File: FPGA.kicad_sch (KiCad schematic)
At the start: 8 parts, among them U3 XC7A100T-FTG256

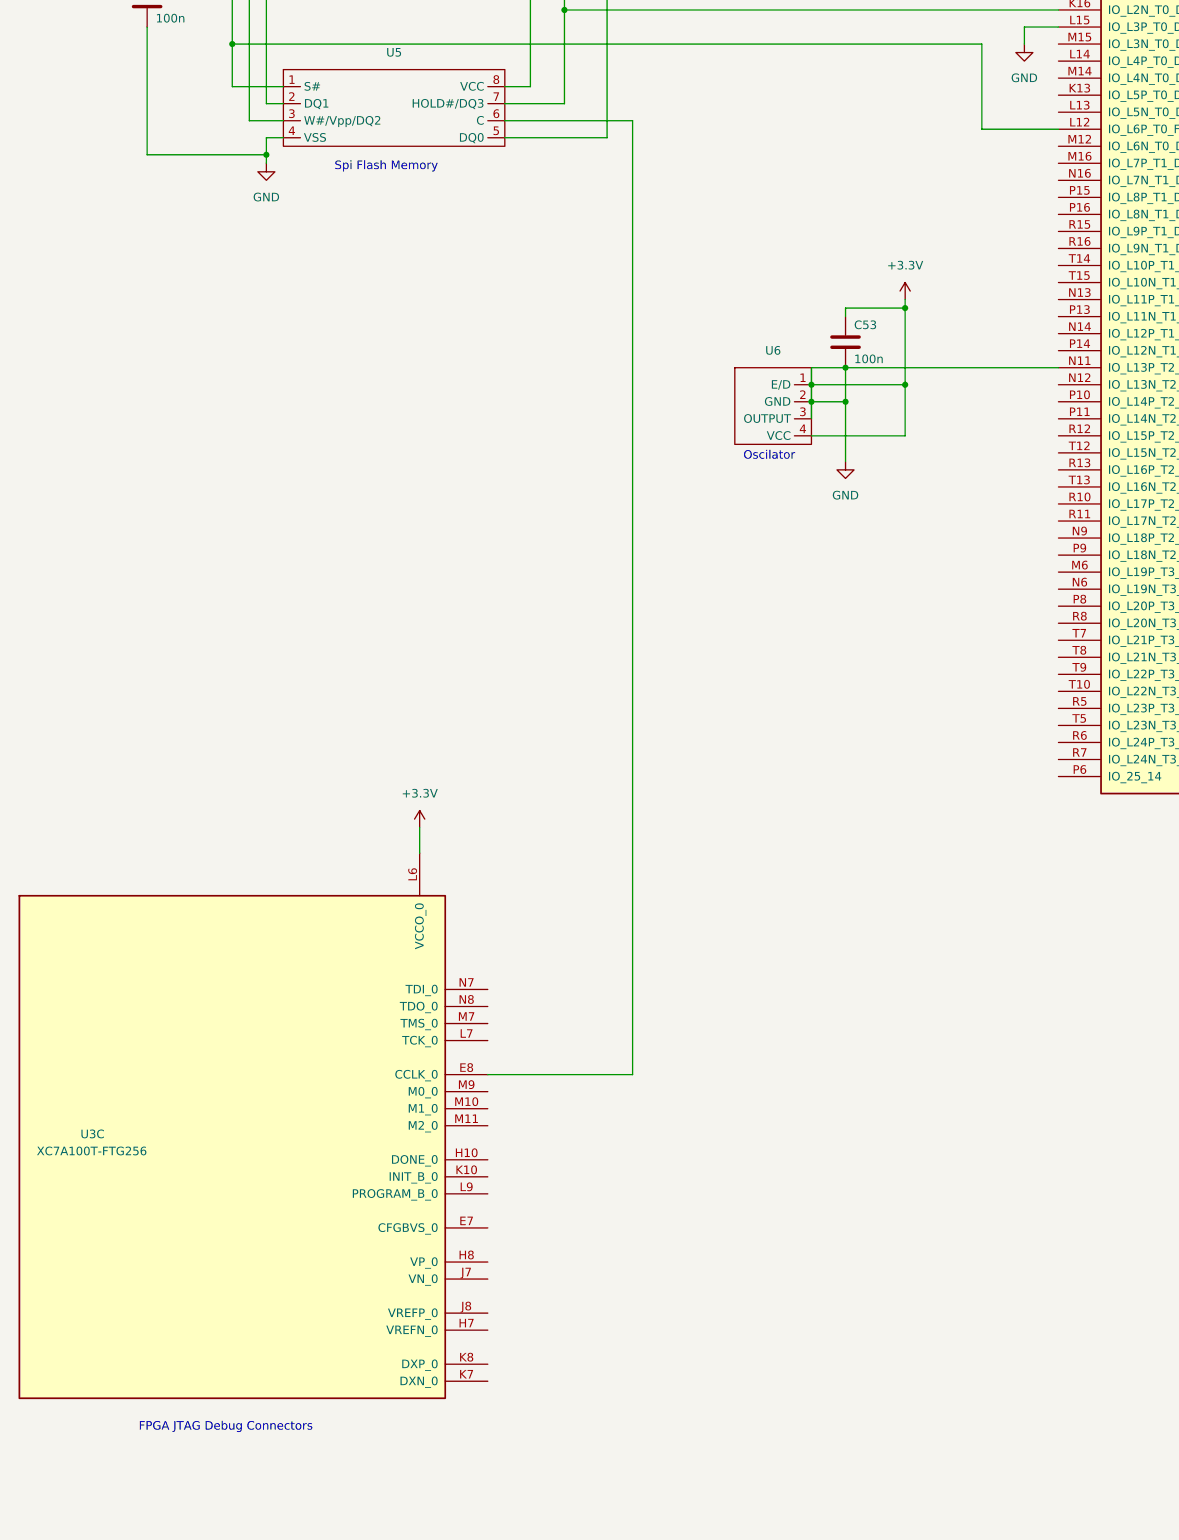
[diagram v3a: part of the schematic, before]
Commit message: Started on FPGA JTAG Connector
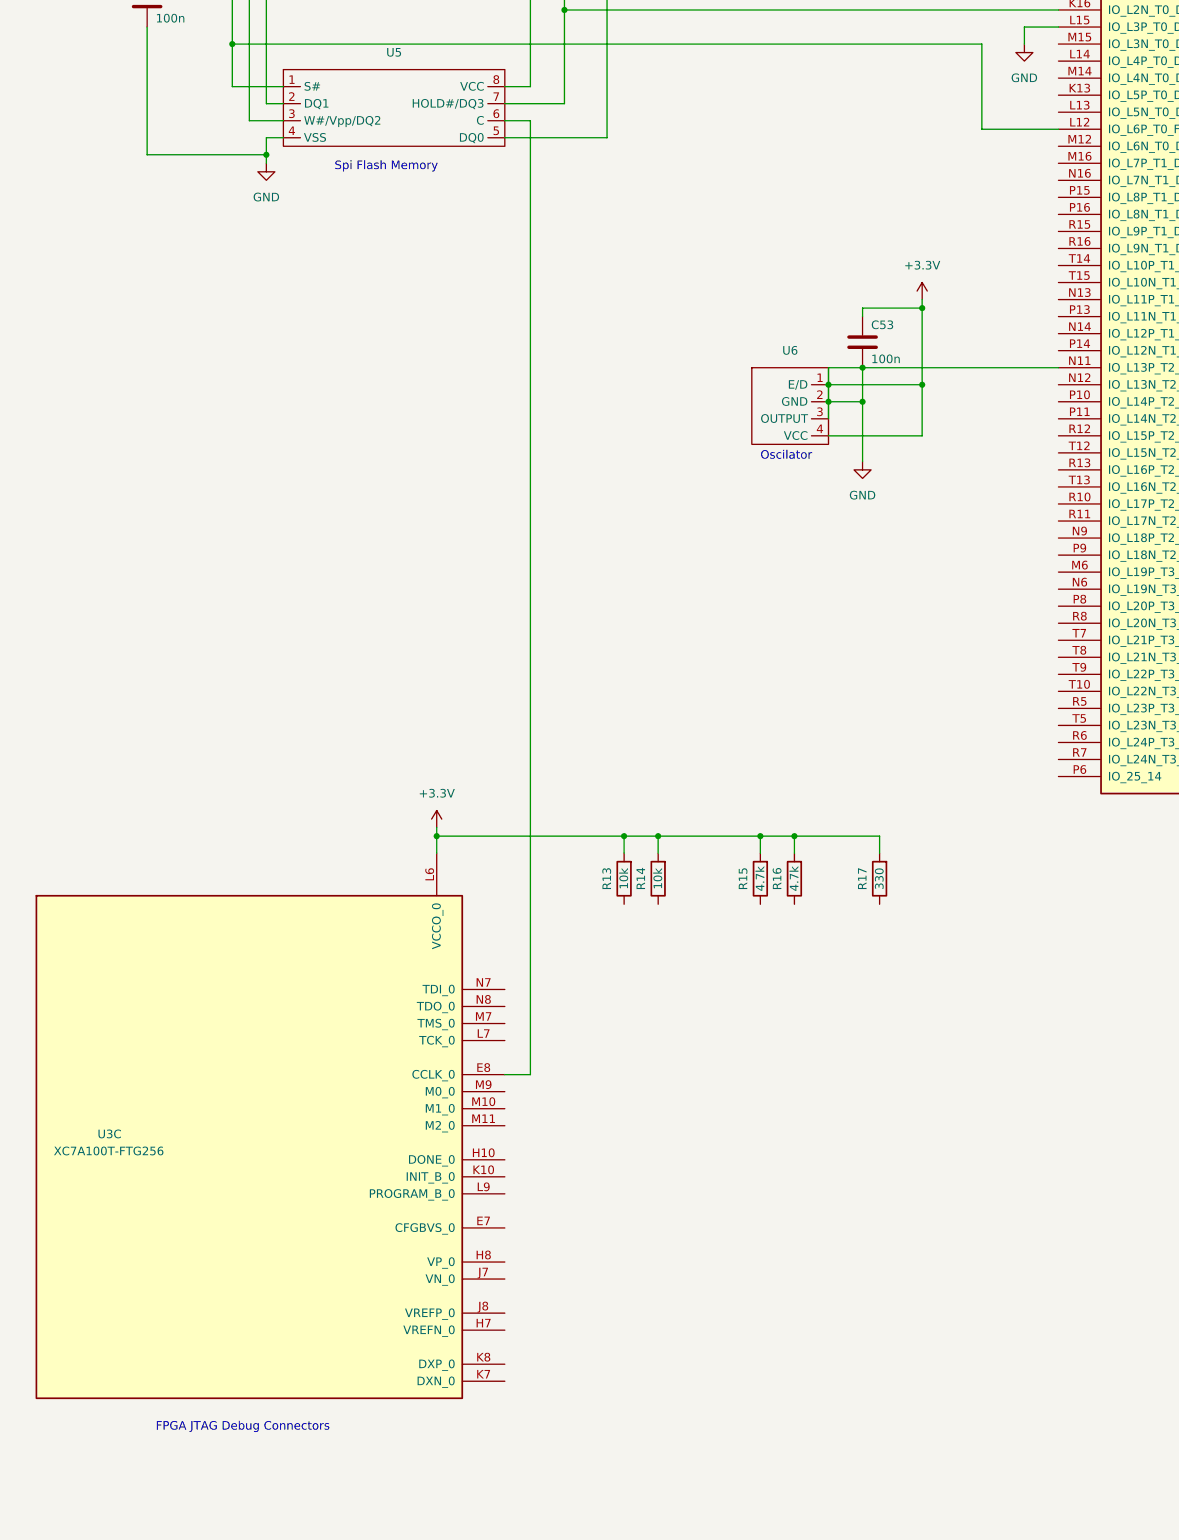
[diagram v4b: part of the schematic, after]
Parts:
- added R13, R14: 10k, symbol Device:R
- added R15, R16: 4.7k, symbol Device:R
- added R17: 330, symbol Device:R
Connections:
- net +3.3V: now also R13.2, R14.2, R15.2, R16.2, R17.2
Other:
- moved on the sheet: C53, U3C, U6

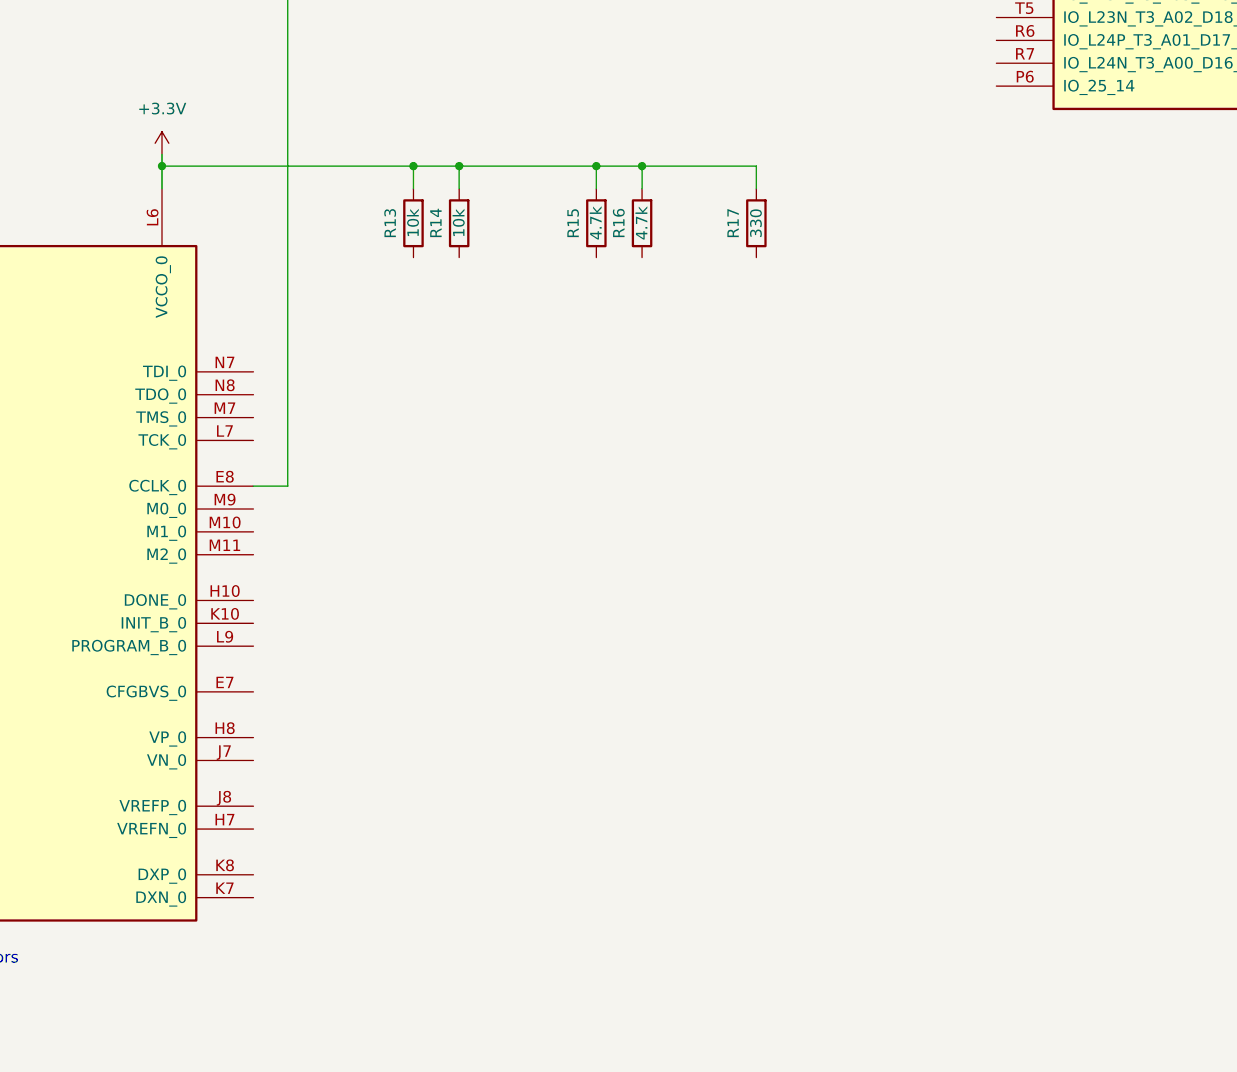
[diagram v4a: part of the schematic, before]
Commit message: Connected JTAG debug connector
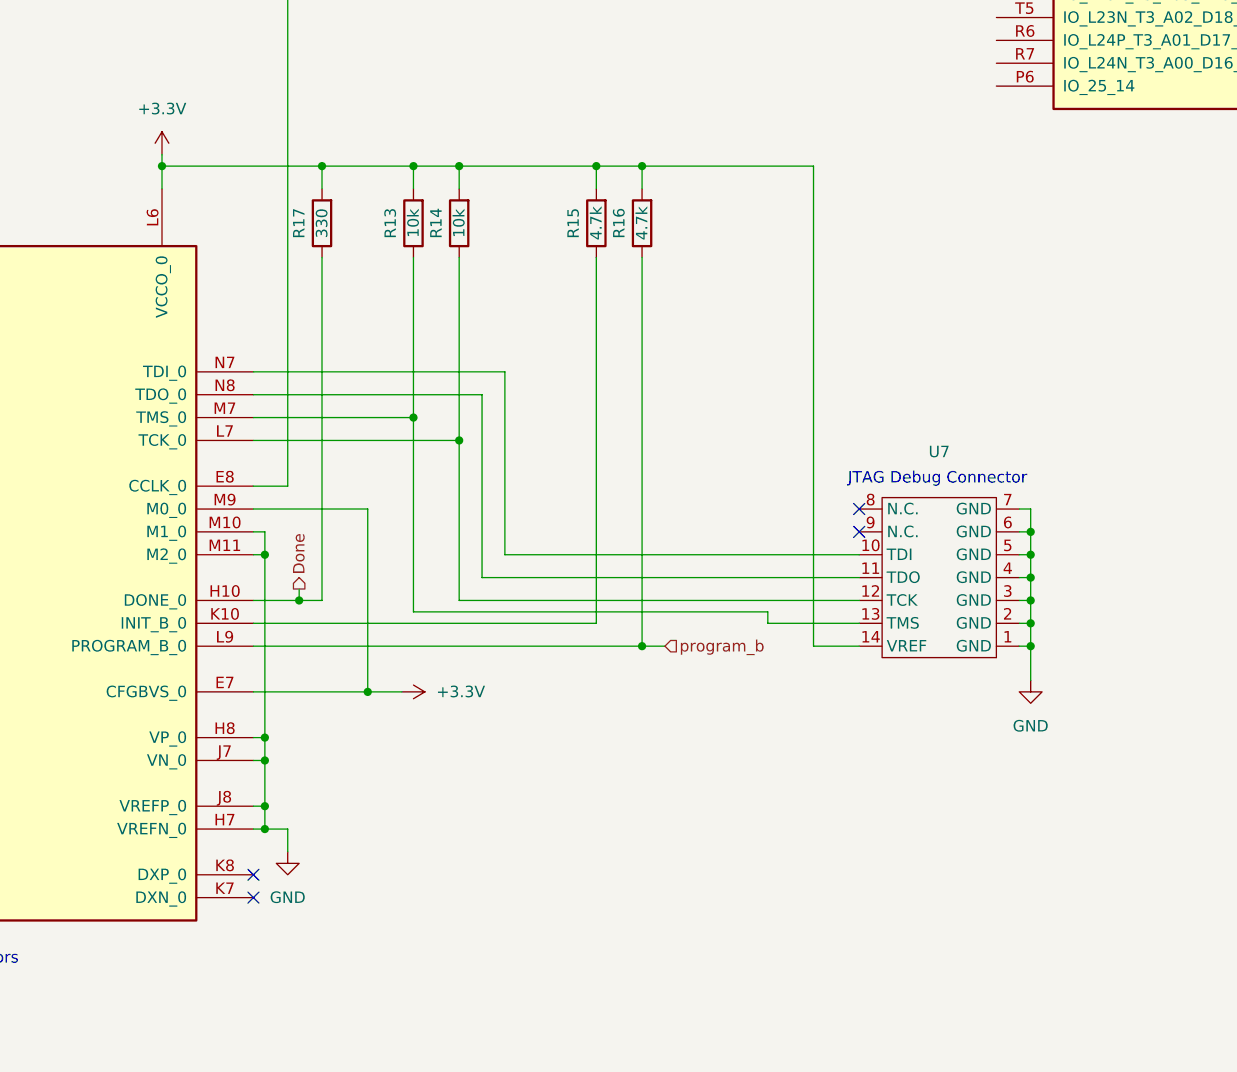
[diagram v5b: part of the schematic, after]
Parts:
- added U7: ~, symbol GuitarZero:FPGA_JTAG_Connector
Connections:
- net +3.3V: now also U3.E7 (CFGBVS_0), U3.H7 (VREFN_0), U3.H8 (VP_0), U3.J7 (VN_0), U3.J8 (VREFP_0), U3.M10 (M1_0), U3.M11 (M2_0), U3.M9 (M0_0), U7.1 (GND), U7.14 (VREF), U7.2 (GND), U7.3 (GND), U7.4 (GND), U7.5 (GND), U7.6 (GND), U7.7 (GND)
- net at R15.1: now also U3.K10 (INIT_B_0)
- net at R14.1: now also U3.L7 (TCK_0), U7.12 (TCK)
- net program_b: now reaches R16.1
- net program_b: now also U3.L9 (PROGRAM_B_0)
- net Done: now reaches R17.1
- net Done: now also U3.H10 (DONE_0)
- net at R13.1: now also U3.M7 (TMS_0), U7.13 (TMS)
- net at U3.N7 (TDI_0): now also U7.10 (TDI)
- net at U3.N8 (TDO_0): now also U7.11 (TDO)
- no-connect marks 120 -> 124
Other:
- note added: "JTAG Debug Connector"

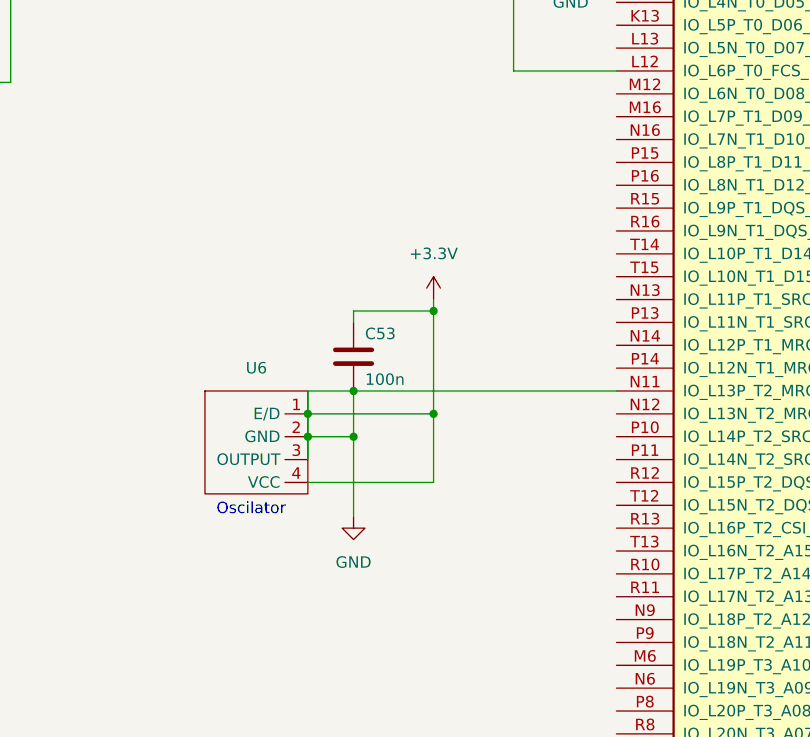
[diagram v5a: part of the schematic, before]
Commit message: Fixed broken oscillator
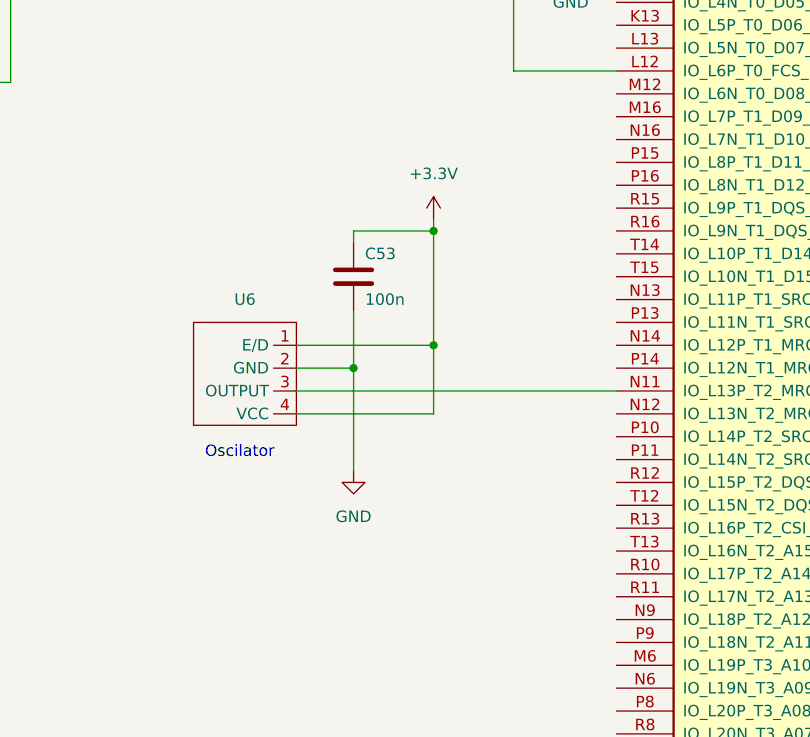
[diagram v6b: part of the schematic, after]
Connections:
- net +3.3V: no longer C52.2, C53.2, U3.A1 (GND), U3.A11 (GND), U3.A16 (VCCO_15), U3.A6 (VCCO_35), U3.B13 (VCCO_15), U3.B3 (VCCO_35), U3.B8 (GND), U3.C10 (VCCO_15), U3.C15 (GND), U3.C5 (GND), U3.D12 (GND), U3.D2 (GND), U3.D7 (VCCO_35), U3.E14 (VCCO_15), U3.E4 (VCCO_35), U3.E9 (GND), U3.F1 (VCCO_35), U3.F10 (GND), U3.F16 (GND), U3.F6 (GND), U3.F8 (VCCBATT_0), U3.G13 (GND), U3.G3 (GND), U3.G7 (GNDADC_0), U3.G9 (GND), U3.H15 (VCCO_15), U3.H6 (GND), U3.H7 (VREFN_0), U3.H8 (VP_0), U3.J11 (GND), U3.J12 (VCCO_15), U3.J2 (VCCO_35), U3.J7 (VN_0), U3.J8 (VREFP_0), U3.J9 (GND), U3.K14 (GND), U3.K4 (GND), U3.K6 (GND), U3.L1 (GND), U3.L11 (GND), U3.L15 (IO_L3P_T0_DQS_PUDC_B_14), U3.M10 (M1_0), U3.M11 (M2_0), U3.M3 (VCCO_34), U3.M8 (GND), U3.N11 (IO_L13P_T2_MRCC_14), U3.N15 (GND), U3.N5 (GND), U3.P12 (GND), U3.P2 (GND), U3.R4 (VCCO_34), U3.R9 (GND), U3.T1 (VCCO_34), U3.T16 (GND), U3.T6 (GND), U5.4 (VSS), U6.2 (GND), U6.3 (OUTPUT), U7.1 (GND), U7.2 (GND), U7.3 (GND), U7.4 (GND), U7.5 (GND), U7.6 (GND), U7.7 (GND)
- new net: U3.N11 (IO_L13P_T2_MRCC_14), U6.3 (OUTPUT)
- new net GND: C52.2, C53.2, U3.A1 (GND), U3.A11 (GND), U3.A16 (VCCO_15), U3.A6 (VCCO_35), U3.B13 (VCCO_15), U3.B3 (VCCO_35), U3.B8 (GND), U3.C10 (VCCO_15), U3.C15 (GND), U3.C5 (GND), U3.D12 (GND), U3.D2 (GND), U3.D7 (VCCO_35), U3.E14 (VCCO_15), U3.E4 (VCCO_35), U3.E9 (GND), U3.F1 (VCCO_35), U3.F10 (GND), U3.F16 (GND), U3.F6 (GND), U3.F8 (VCCBATT_0), U3.G13 (GND), U3.G3 (GND), U3.G7 (GNDADC_0), U3.G9 (GND), U3.H15 (VCCO_15), U3.H6 (GND), U3.H7 (VREFN_0), U3.H8 (VP_0), U3.J11 (GND), U3.J12 (VCCO_15), U3.J2 (VCCO_35), U3.J7 (VN_0), U3.J8 (VREFP_0), U3.J9 (GND), U3.K14 (GND), U3.K4 (GND), U3.K6 (GND), U3.L1 (GND), U3.L11 (GND), U3.L15 (IO_L3P_T0_DQS_PUDC_B_14), U3.M10 (M1_0), U3.M11 (M2_0), U3.M3 (VCCO_34), U3.M8 (GND), U3.N15 (GND), U3.N5 (GND), U3.P12 (GND), U3.P2 (GND), U3.R4 (VCCO_34), U3.R9 (GND), U3.T1 (VCCO_34), U3.T16 (GND), U3.T6 (GND), U5.4 (VSS), U6.2 (GND), U7.1 (GND), U7.2 (GND), U7.3 (GND), U7.4 (GND), U7.5 (GND), U7.6 (GND), U7.7 (GND)
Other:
- moved on the sheet: C53

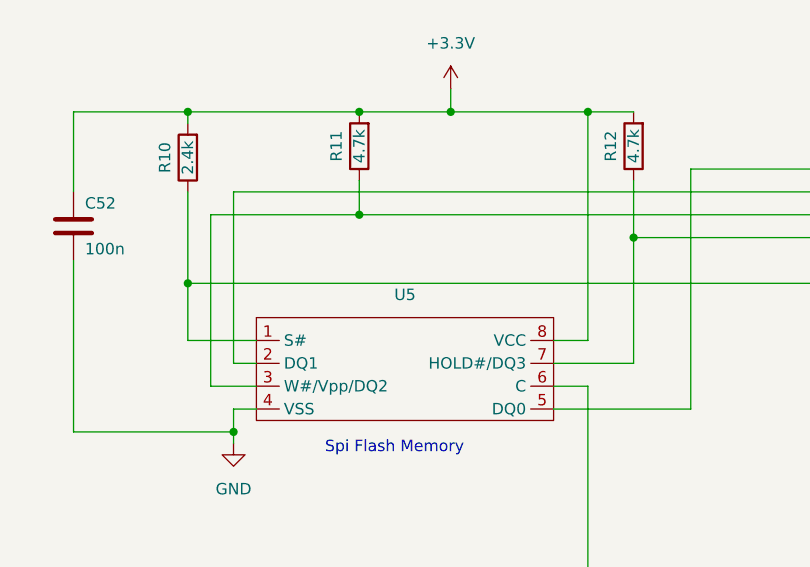
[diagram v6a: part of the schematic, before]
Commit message: Added AudioJack
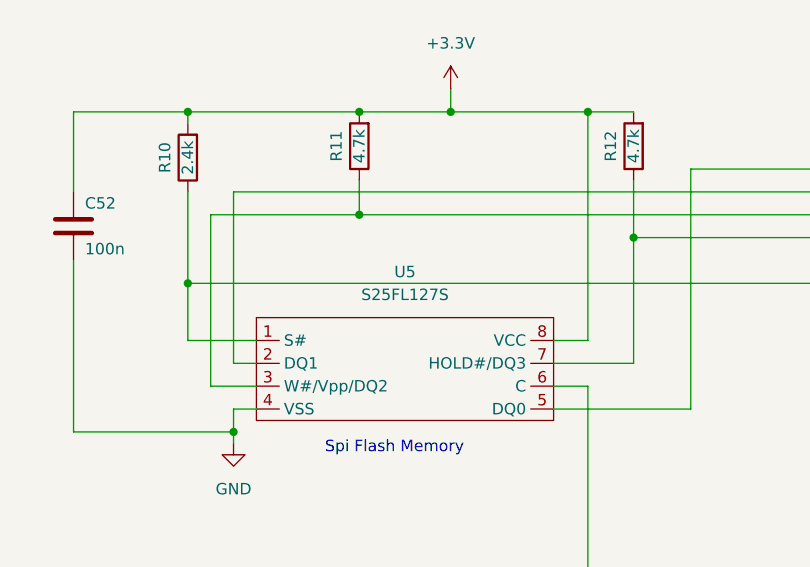
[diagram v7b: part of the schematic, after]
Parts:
- removed U5: ~, symbol GuitarZero:SpiFlashPlaceholder
- added U5: S25FL127S, symbol GuitarZero:S25FL127S
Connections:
- net +3.3V: now also U5.8 (VCC)
- net GND: now also U5.4 (VSS)
- net at U3.J13 (IO_L1P_T0_D00_MOSI_14): now also U5.5 (DQ0)
- net at U3.J14 (IO_L1N_T0_D01_DIN_14): now also U5.2 (DQ1)
- net at R11.1, U3.K15 (IO_L2P_T0_D02_14): now also U5.3 (W#/Vpp/DQ2)
- net at R12.1, U3.K16 (IO_L2N_T0_D03_14): now also U5.7 (HOLD#/DQ3)
- net at R10.1, U3.L12 (IO_L6P_T0_FCS_B_14): now also U5.1 (S#)
- net at U3.E8 (CCLK_0): now also U5.6 (C)
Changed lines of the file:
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@@
+    )
+  )
+  (symbol (lib_id "GuitarZero:S25FL127S") (at 85.09 72.39 0) (unit 1)
+    (in_bom yes) (on_board yes) (dnp no) (fields_autoplaced)
+    (property "Reference" "U5" (at 85.09 63.5 0)
+      (effects (font (size 1.27 1.27)))
+    )
+    (property "Value" "S25FL127S" (at 85.09 66.04 0)
+      (effects (font (size 1.27 1.27)))
+    )
+    (property "Footprint" "" (at 77.47 72.39 0)
+      (effects (font (size 1.27 1.27)) hide)
+    )
+    (property "Datasheet" "" (at 77.47 72.39 0)
+      (effects (font (size 1.27 1.27)) hide)
+    )
+    (pin "1")
+    (pin "2")
+    (pin "3")
+    (pin "4")
+    (pin "5")
+    (pin "6")
+    (pin "7")
+    (pin "8")
+    (instances
+      (project "GuitarZero"
+        (path "/fba50eda-8593-4456-af98-ff56fd418a76/7788bc9b-1e55-4835-b7d3-ea790efb8c61"
+          (reference "U5") (unit 1)
+        )
+      )
     )
   )
@@
         )
       )
-    )
-  )
-  (symbol (lib_id "GuitarZero:SpiFlashPlaceholder") (at 85.09 72.39 0) (unit 1)
-    (in_bom yes) (on_board yes) (dnp no) (fields_autoplaced)
-    (property "Reference" "U5" (at 85.09 66.04 0)
-      (effects (font (size 1.27 1.27)))
-    )
-    (property "Value" "~" (at 77.47 72.39 0)
-      (effects (font (size 1.27 1.27)))
-    )
-    (property "Footprint" "" (at 77.47 72.39 0)
-      (effects (font (size 1.27 1.27)) hide)
-    )
-    (property "Datasheet" "" (at 77.47 72.39 0)
-      (effects (font (size 1.27 1.27)) hide)
-    )
-    (pin "1")
-    (pin "2")
-    (pin "3")
-    (pin "4")
-    (pin "5")
-    (pin "6")
-    (pin "7")
-    (pin "8")
-    (instances
-      (project "GuitarZero"
-        (path "/fba50eda-8593-4456-af98-ff56fd418a76/7788bc9b-1e55-4835-b7d3-ea790efb8c61"
-          (reference "U5") (unit 1)
-        )
-      )
